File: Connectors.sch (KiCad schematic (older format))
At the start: 4 parts

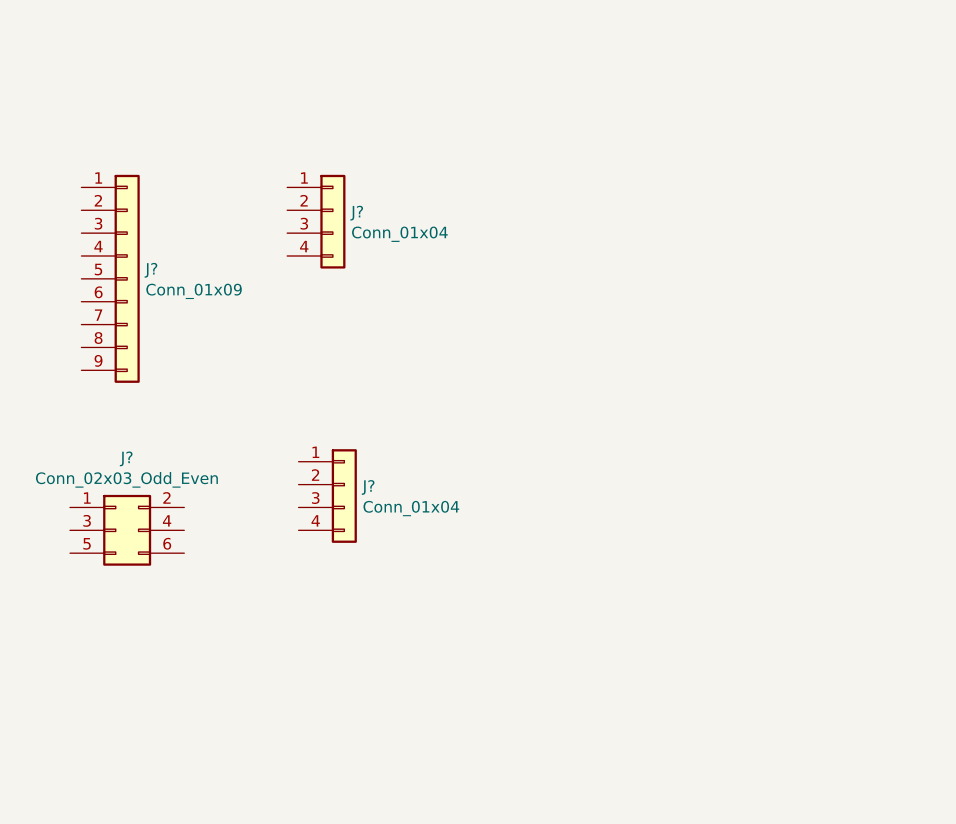
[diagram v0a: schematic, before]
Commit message: Arranged symbols.
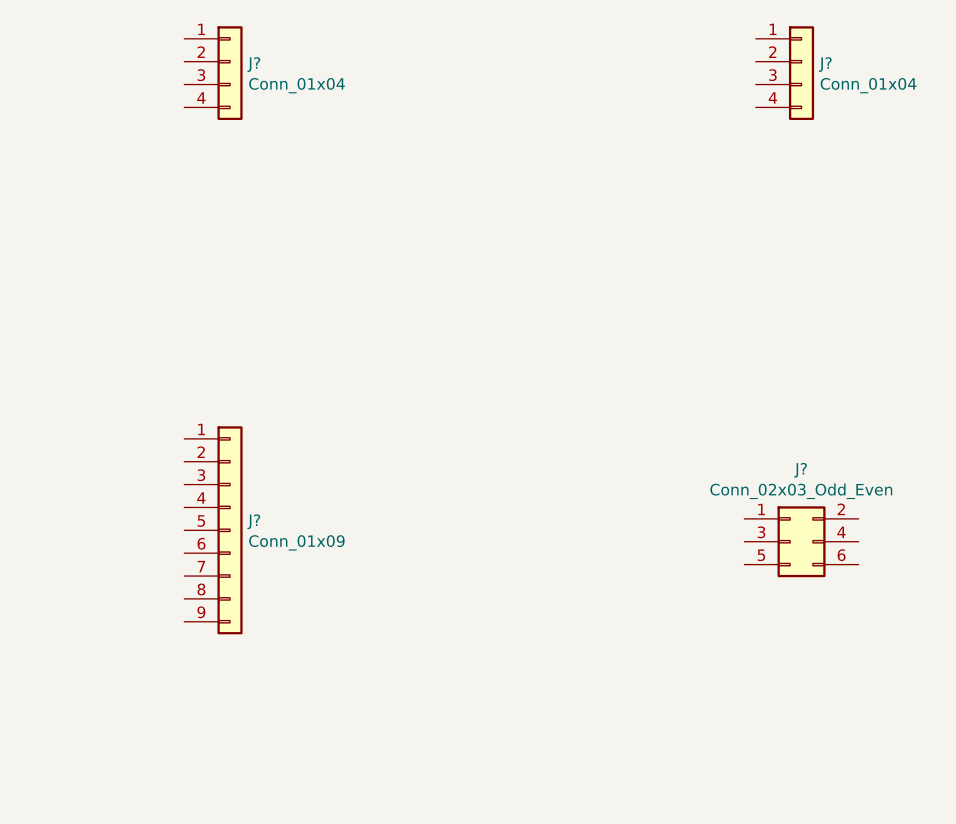
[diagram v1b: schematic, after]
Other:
- moved on the sheet: J?
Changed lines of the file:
@@
 L Connector_Generic:Conn_02x03_Odd_Even J?
 U 1 1 5D848220
-P 4150 3950
-F 0 "J?" H 4200 4267 50  0000 C CNN
-F 1 "Conn_02x03_Odd_Even" H 4200 4176 50  0000 C CNN
-F 2 "" H 4150 3950 50  0001 C CNN
-F 3 "~" H 4150 3950 50  0001 C CNN
-	1    4150 3950
+P 7100 4000
+F 0 "J?" H 7150 4317 50  0000 C CNN
+F 1 "Conn_02x03_Odd_Even" H 7150 4226 50  0000 C CNN
+F 2 "" H 7100 4000 50  0001 C CNN
+F 3 "~" H 7100 4000 50  0001 C CNN
+	1    7100 4000
 	1    0    0    -1
 $EndComp
@@
 L Connector_Generic:Conn_01x04 J?
 U 1 1 5D848B48
-P 5100 2550
-F 0 "J?" H 5180 2542 50  0000 L CNN
-F 1 "Conn_01x04" H 5180 2451 50  0000 L CNN
-F 2 "" H 5100 2550 50  0001 C CNN
-F 3 "~" H 5100 2550 50  0001 C CNN
-	1    5100 2550
+P 4650 1900
+F 0 "J?" H 4730 1892 50  0000 L CNN
+F 1 "Conn_01x04" H 4730 1801 50  0000 L CNN
+F 2 "" H 4650 1900 50  0001 C CNN
+F 3 "~" H 4650 1900 50  0001 C CNN
+	1    4650 1900
 	1    0    0    -1
 $EndComp
@@
 L Connector_Generic:Conn_01x09 J?
 U 1 1 5D8491A9
-P 4200 2850
-F 0 "J?" H 4280 2892 50  0000 L CNN
-F 1 "Conn_01x09" H 4280 2801 50  0000 L CNN
-F 2 "" H 4200 2850 50  0001 C CNN
-F 3 "~" H 4200 2850 50  0001 C CNN
-	1    4200 2850
+P 4650 3950
+F 0 "J?" H 4730 3992 50  0000 L CNN
+F 1 "Conn_01x09" H 4730 3901 50  0000 L CNN
+F 2 "" H 4650 3950 50  0001 C CNN
+F 3 "~" H 4650 3950 50  0001 C CNN
+	1    4650 3950
 	1    0    0    -1
 $EndComp
@@
 L Connector_Generic:Conn_01x04 J?
 U 1 1 5D849E1D
-P 5150 3750
-F 0 "J?" H 5230 3742 50  0000 L CNN
-F 1 "Conn_01x04" H 5230 3651 50  0000 L CNN
-F 2 "" H 5150 3750 50  0001 C CNN
-F 3 "~" H 5150 3750 50  0001 C CNN
-	1    5150 3750
+P 7150 1900
+F 0 "J?" H 7230 1892 50  0000 L CNN
+F 1 "Conn_01x04" H 7230 1801 50  0000 L CNN
+F 2 "" H 7150 1900 50  0001 C CNN
+F 3 "~" H 7150 1900 50  0001 C CNN
+	1    7150 1900
 	1    0    0    -1
 $EndComp

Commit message: Anottated.
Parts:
- gave numbers to parts that had none: 4
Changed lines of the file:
@@
 $EndDescr
 $Comp
-L Connector_Generic:Conn_02x03_Odd_Even J?
+L Connector_Generic:Conn_02x03_Odd_Even J3
 U 1 1 5D848220
 P 7100 4000
-F 0 "J?" H 7150 4317 50  0000 C CNN
+F 0 "J3" H 7150 4317 50  0000 C CNN
 F 1 "Conn_02x03_Odd_Even" H 7150 4226 50  0000 C CNN
 F 2 "" H 7100 4000 50  0001 C CNN
@@
 $EndComp
 $Comp
-L Connector_Generic:Conn_01x04 J?
+L Connector_Generic:Conn_01x04 J1
 U 1 1 5D848B48
 P 4650 1900
-F 0 "J?" H 4730 1892 50  0000 L CNN
+F 0 "J1" H 4730 1892 50  0000 L CNN
 F 1 "Conn_01x04" H 4730 1801 50  0000 L CNN
 F 2 "" H 4650 1900 50  0001 C CNN
@@
 $EndComp
 $Comp
-L Connector_Generic:Conn_01x09 J?
+L Connector_Generic:Conn_01x09 J2
 U 1 1 5D8491A9
 P 4650 3950
-F 0 "J?" H 4730 3992 50  0000 L CNN
+F 0 "J2" H 4730 3992 50  0000 L CNN
 F 1 "Conn_01x09" H 4730 3901 50  0000 L CNN
 F 2 "" H 4650 3950 50  0001 C CNN
@@
 $EndComp
 $Comp
-L Connector_Generic:Conn_01x04 J?
+L Connector_Generic:Conn_01x04 J4
 U 1 1 5D849E1D
 P 7150 1900
-F 0 "J?" H 7230 1892 50  0000 L CNN
+F 0 "J4" H 7230 1892 50  0000 L CNN
 F 1 "Conn_01x04" H 7230 1801 50  0000 L CNN
 F 2 "" H 7150 1900 50  0001 C CNN

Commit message: Added footprints assigments.
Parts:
- J1, J4: footprint (none) -> Connector_PinSocket_2.54mm:PinSocket_1x04_P2.54mm_Vertical
- J2: footprint (none) -> Connector_PinSocket_2.54mm:PinSocket_1x09_P2.54mm_Vertical
- J3: footprint (none) -> Connector_PinSocket_2.54mm:PinSocket_2x03_P2.54mm_Vertical
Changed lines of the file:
@@
 F 0 "J3" H 7150 4317 50  0000 C CNN
 F 1 "Conn_02x03_Odd_Even" H 7150 4226 50  0000 C CNN
-F 2 "" H 7100 4000 50  0001 C CNN
+F 2 "Connector_PinSocket_2.54mm:PinSocket_2x03_P2.54mm_Vertical" H 7100 4000 50  0001 C CNN
 F 3 "~" H 7100 4000 50  0001 C CNN
 	1    7100 4000
@@
 F 0 "J1" H 4730 1892 50  0000 L CNN
 F 1 "Conn_01x04" H 4730 1801 50  0000 L CNN
-F 2 "" H 4650 1900 50  0001 C CNN
+F 2 "Connector_PinSocket_2.54mm:PinSocket_1x04_P2.54mm_Vertical" H 4650 1900 50  0001 C CNN
 F 3 "~" H 4650 1900 50  0001 C CNN
 	1    4650 1900
@@
 F 0 "J2" H 4730 3992 50  0000 L CNN
 F 1 "Conn_01x09" H 4730 3901 50  0000 L CNN
-F 2 "" H 4650 3950 50  0001 C CNN
+F 2 "Connector_PinSocket_2.54mm:PinSocket_1x09_P2.54mm_Vertical" H 4650 3950 50  0001 C CNN
 F 3 "~" H 4650 3950 50  0001 C CNN
 	1    4650 3950
@@
 F 0 "J4" H 7230 1892 50  0000 L CNN
 F 1 "Conn_01x04" H 7230 1801 50  0000 L CNN
-F 2 "" H 7150 1900 50  0001 C CNN
+F 2 "Connector_PinSocket_2.54mm:PinSocket_1x04_P2.54mm_Vertical" H 7150 1900 50  0001 C CNN
 F 3 "~" H 7150 1900 50  0001 C CNN
 	1    7150 1900

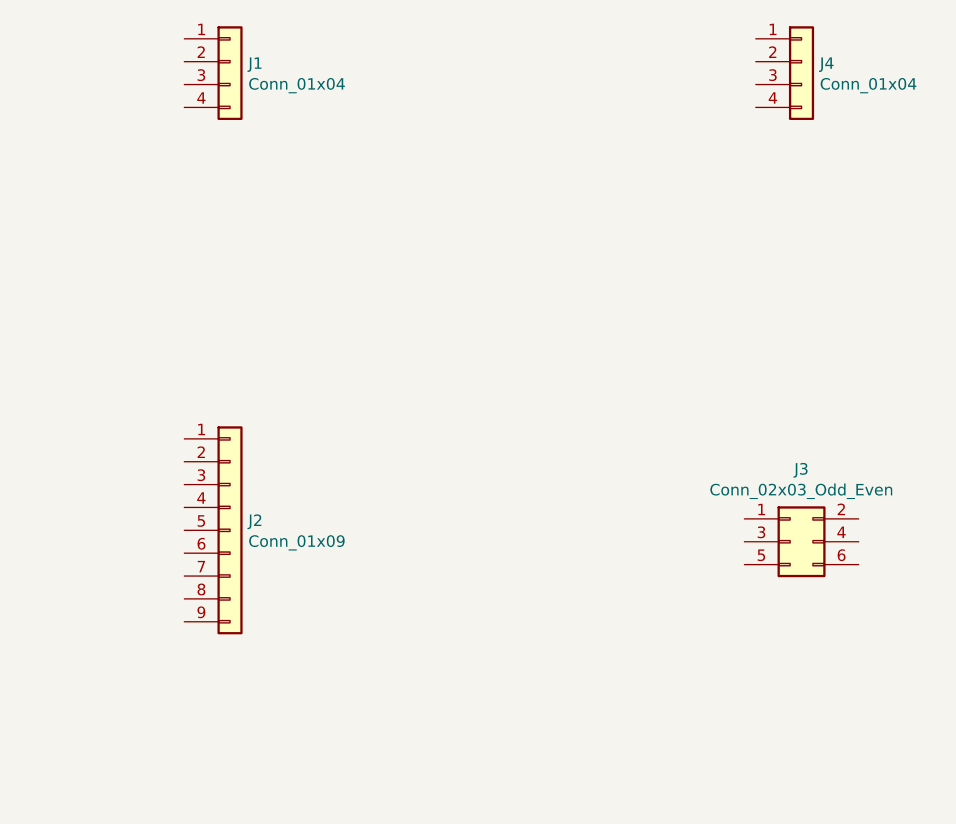
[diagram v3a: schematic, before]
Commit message: Completed asociations and added component values.
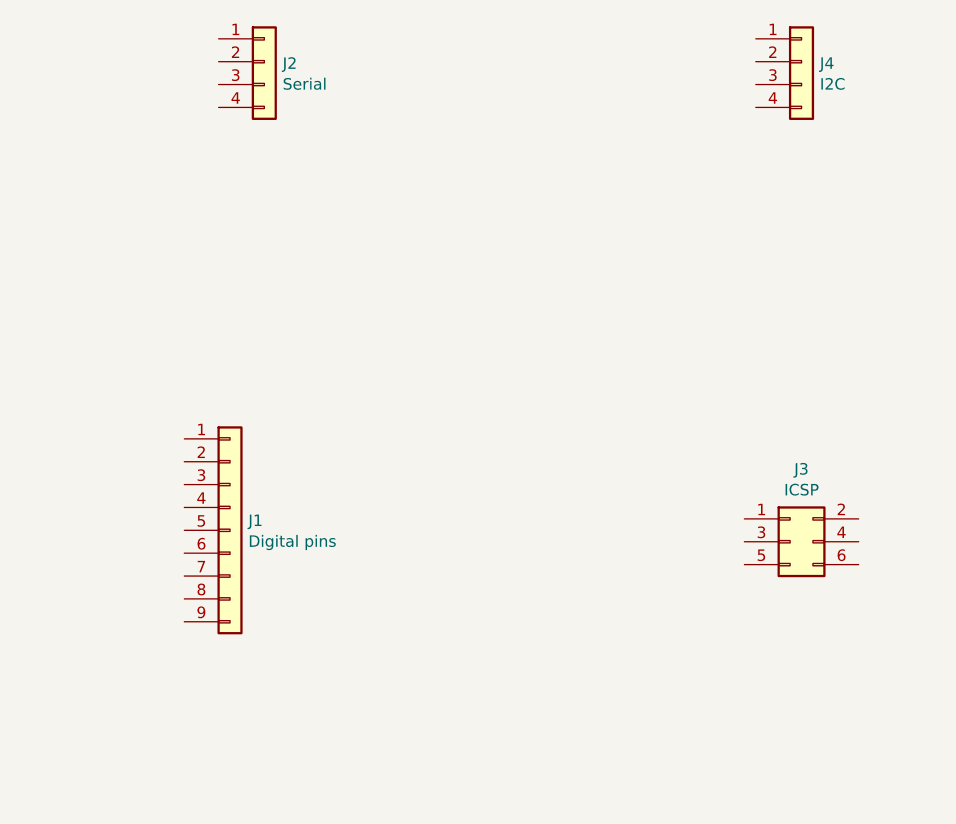
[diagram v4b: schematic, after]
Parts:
- J1: renamed from J2; value Conn_01x09 -> Digital pins
- J2: renamed from J1; value Conn_01x04 -> Serial
- J3: value Conn_02x03_Odd_Even -> ICSP
- J4: value Conn_01x04 -> I2C
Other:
- moved on the sheet: J2
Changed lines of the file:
@@
 P 7100 4000
 F 0 "J3" H 7150 4317 50  0000 C CNN
-F 1 "Conn_02x03_Odd_Even" H 7150 4226 50  0000 C CNN
+F 1 "ICSP" H 7150 4226 50  0000 C CNN
 F 2 "Connector_PinSocket_2.54mm:PinSocket_2x03_P2.54mm_Vertical" H 7100 4000 50  0001 C CNN
 F 3 "~" H 7100 4000 50  0001 C CNN
@@
 $EndComp
 $Comp
-L Connector_Generic:Conn_01x04 J1
+L Connector_Generic:Conn_01x04 J2
 U 1 1 5D848B48
-P 4650 1900
-F 0 "J1" H 4730 1892 50  0000 L CNN
-F 1 "Conn_01x04" H 4730 1801 50  0000 L CNN
-F 2 "Connector_PinSocket_2.54mm:PinSocket_1x04_P2.54mm_Vertical" H 4650 1900 50  0001 C CNN
-F 3 "~" H 4650 1900 50  0001 C CNN
-	1    4650 1900
+P 4800 1900
+F 0 "J2" H 4880 1892 50  0000 L CNN
+F 1 "Serial" H 4880 1801 50  0000 L CNN
+F 2 "Connector_PinSocket_2.54mm:PinSocket_1x04_P2.54mm_Vertical" H 4800 1900 50  0001 C CNN
+F 3 "~" H 4800 1900 50  0001 C CNN
+	1    4800 1900
 	1    0    0    -1
 $EndComp
 $Comp
-L Connector_Generic:Conn_01x09 J2
+L Connector_Generic:Conn_01x09 J1
 U 1 1 5D8491A9
 P 4650 3950
-F 0 "J2" H 4730 3992 50  0000 L CNN
-F 1 "Conn_01x09" H 4730 3901 50  0000 L CNN
+F 0 "J1" H 4730 3992 50  0000 L CNN
+F 1 "Digital pins" H 4730 3901 50  0000 L CNN
 F 2 "Connector_PinSocket_2.54mm:PinSocket_1x09_P2.54mm_Vertical" H 4650 3950 50  0001 C CNN
 F 3 "~" H 4650 3950 50  0001 C CNN
@@
 P 7150 1900
 F 0 "J4" H 7230 1892 50  0000 L CNN
-F 1 "Conn_01x04" H 7230 1801 50  0000 L CNN
+F 1 "I2C" H 7230 1801 50  0000 L CNN
 F 2 "Connector_PinSocket_2.54mm:PinSocket_1x04_P2.54mm_Vertical" H 7150 1900 50  0001 C CNN
 F 3 "~" H 7150 1900 50  0001 C CNN

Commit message: Completed wiring and connectors sheet.
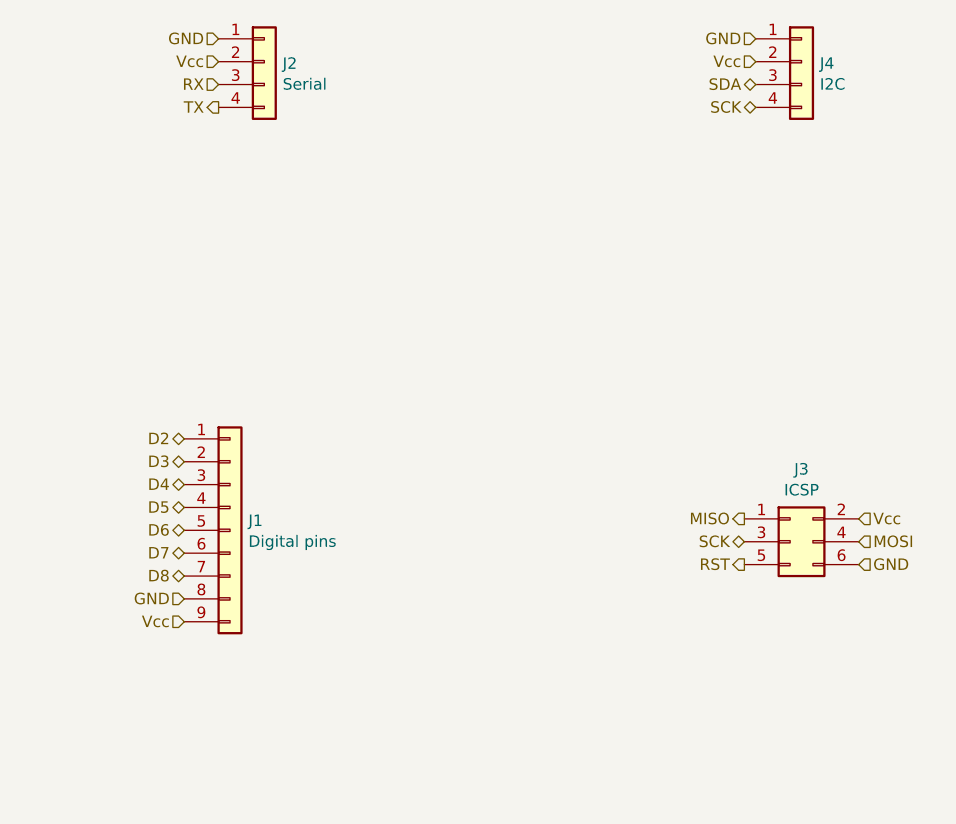
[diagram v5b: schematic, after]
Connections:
- net MISO: now reaches J3.1 (Pin_1)
- net Vcc: now reaches J3.2 (Pin_2)
- net Vcc: now also J1.9 (Pin_9), J2.2 (Pin_2), J4.2 (Pin_2)
- net SCK: now reaches J3.3 (Pin_3)
- net SCK: now also J4.4 (Pin_4)
- net MOSI: now reaches J3.4 (Pin_4)
- net RST: now reaches J3.5 (Pin_5)
- net GND: now reaches J3.6 (Pin_6)
- net GND: now also J1.8 (Pin_8), J2.1 (Pin_1), J4.1 (Pin_1)
- net RX: now reaches J2.3 (Pin_3)
- net TX: now reaches J2.4 (Pin_4)
- net D2: now reaches J1.1 (Pin_1)
- net D3: now reaches J1.2 (Pin_2)
- net D4: now reaches J1.3 (Pin_3)
- net D5: now reaches J1.4 (Pin_4)
- net D6: now reaches J1.5 (Pin_5)
- net D7: now reaches J1.6 (Pin_6)
- net D8: now reaches J1.7 (Pin_7)
- net SDA: now reaches J4.3 (Pin_3)
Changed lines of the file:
@@
 	1    0    0    -1
 $EndComp
+Text HLabel 6900 3900 0    50   Output ~ 0
+MISO
+Text HLabel 6900 4000 0    50   BiDi ~ 0
+SCK
+Text HLabel 6900 4100 0    50   Output ~ 0
+RST
+Text HLabel 7400 3900 2    50   Input ~ 0
+Vcc
+Text HLabel 7400 4000 2    50   Input ~ 0
+MOSI
+Text HLabel 7400 4100 2    50   Input ~ 0
+GND
+Text HLabel 4600 1800 0    50   Input ~ 0
+GND
+Text HLabel 4600 1900 0    50   Input ~ 0
+Vcc
+Text HLabel 4600 2000 0    50   Input ~ 0
+RX
+Text HLabel 4600 2100 0    50   Output ~ 0
+TX
+Text HLabel 6950 1800 0    50   Input ~ 0
+GND
+Text HLabel 6950 1900 0    50   Input ~ 0
+Vcc
+Text HLabel 6950 2000 0    50   BiDi ~ 0
+SDA
+Text HLabel 4450 3550 0    50   BiDi ~ 0
+D2
+Text HLabel 4450 3650 0    50   BiDi ~ 0
+D3
+Text HLabel 4450 3750 0    50   BiDi ~ 0
+D4
+Text HLabel 4450 3850 0    50   BiDi ~ 0
+D5
+Text HLabel 4450 3950 0    50   BiDi ~ 0
+D6
+Text HLabel 4450 4050 0    50   BiDi ~ 0
+D7
+Text HLabel 4450 4150 0    50   BiDi ~ 0
+D8
+Text HLabel 4450 4250 0    50   Input ~ 0
+GND
+Text HLabel 4450 4350 0    50   Input ~ 0
+Vcc
+Text HLabel 6950 2100 0    50   BiDi ~ 0
+SCK
 $EndSCHEMATC

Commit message: Added functional block description.
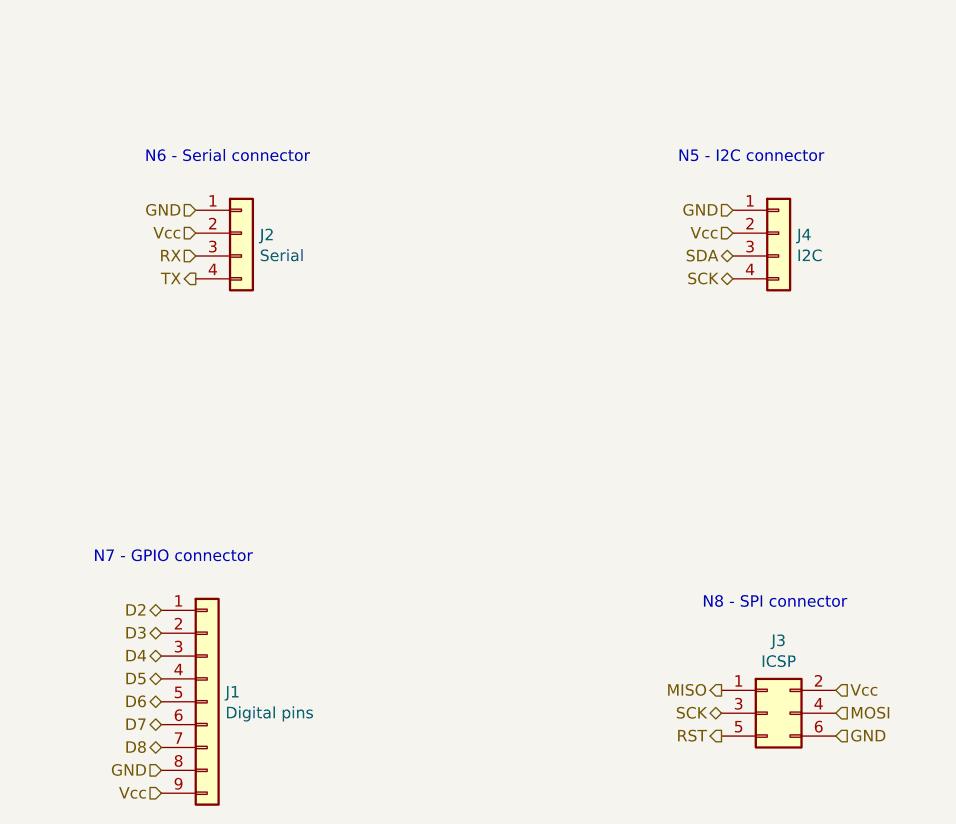
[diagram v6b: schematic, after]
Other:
- note added: "N5 - I2C connector"
- note added: "N6 - Serial connector\n"
- note added: "N7 - GPIO connector"
- note added: "N8 - SPI connector"
- moved on the sheet: J1, J2, J3, J4
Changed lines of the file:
@@
 L Connector_Generic:Conn_02x03_Odd_Even J3
 U 1 1 5D848220
-P 7100 4000
-F 0 "J3" H 7150 4317 50  0000 C CNN
-F 1 "ICSP" H 7150 4226 50  0000 C CNN
-F 2 "Connector_PinSocket_2.54mm:PinSocket_2x03_P2.54mm_Vertical" H 7100 4000 50  0001 C CNN
-F 3 "~" H 7100 4000 50  0001 C CNN
-	1    7100 4000
+P 7000 4750
+F 0 "J3" H 7050 5067 50  0000 C CNN
+F 1 "ICSP" H 7050 4976 50  0000 C CNN
+F 2 "Connector_PinSocket_2.54mm:PinSocket_2x03_P2.54mm_Vertical" H 7000 4750 50  0001 C CNN
+F 3 "~" H 7000 4750 50  0001 C CNN
+	1    7000 4750
 	1    0    0    -1
 $EndComp
@@
 L Connector_Generic:Conn_01x04 J2
 U 1 1 5D848B48
-P 4800 1900
-F 0 "J2" H 4880 1892 50  0000 L CNN
-F 1 "Serial" H 4880 1801 50  0000 L CNN
-F 2 "Connector_PinSocket_2.54mm:PinSocket_1x04_P2.54mm_Vertical" H 4800 1900 50  0001 C CNN
-F 3 "~" H 4800 1900 50  0001 C CNN
-	1    4800 1900
+P 4700 2650
+F 0 "J2" H 4780 2642 50  0000 L CNN
+F 1 "Serial" H 4780 2551 50  0000 L CNN
+F 2 "Connector_PinSocket_2.54mm:PinSocket_1x04_P2.54mm_Vertical" H 4700 2650 50  0001 C CNN
+F 3 "~" H 4700 2650 50  0001 C CNN
+	1    4700 2650
 	1    0    0    -1
 $EndComp
@@
 L Connector_Generic:Conn_01x09 J1
 U 1 1 5D8491A9
-P 4650 3950
-F 0 "J1" H 4730 3992 50  0000 L CNN
-F 1 "Digital pins" H 4730 3901 50  0000 L CNN
-F 2 "Connector_PinSocket_2.54mm:PinSocket_1x09_P2.54mm_Vertical" H 4650 3950 50  0001 C CNN
-F 3 "~" H 4650 3950 50  0001 C CNN
-	1    4650 3950
+P 4550 4700
+F 0 "J1" H 4630 4742 50  0000 L CNN
+F 1 "Digital pins" H 4630 4651 50  0000 L CNN
+F 2 "Connector_PinSocket_2.54mm:PinSocket_1x09_P2.54mm_Vertical" H 4550 4700 50  0001 C CNN
+F 3 "~" H 4550 4700 50  0001 C CNN
+	1    4550 4700
 	1    0    0    -1
 $EndComp
@@
 L Connector_Generic:Conn_01x04 J4
 U 1 1 5D849E1D
-P 7150 1900
-F 0 "J4" H 7230 1892 50  0000 L CNN
-F 1 "I2C" H 7230 1801 50  0000 L CNN
-F 2 "Connector_PinSocket_2.54mm:PinSocket_1x04_P2.54mm_Vertical" H 7150 1900 50  0001 C CNN
-F 3 "~" H 7150 1900 50  0001 C CNN
-	1    7150 1900
+P 7050 2650
+F 0 "J4" H 7130 2642 50  0000 L CNN
+F 1 "I2C" H 7130 2551 50  0000 L CNN
+F 2 "Connector_PinSocket_2.54mm:PinSocket_1x04_P2.54mm_Vertical" H 7050 2650 50  0001 C CNN
+F 3 "~" H 7050 2650 50  0001 C CNN
+	1    7050 2650
 	1    0    0    -1
 $EndComp
-Text HLabel 6900 3900 0    50   Output ~ 0
+Text HLabel 6800 4650 0    50   Output ~ 0
 MISO
-Text HLabel 6900 4000 0    50   BiDi ~ 0
+Text HLabel 6800 4750 0    50   BiDi ~ 0
 SCK
-Text HLabel 6900 4100 0    50   Output ~ 0
+Text HLabel 6800 4850 0    50   Output ~ 0
 RST
-Text HLabel 7400 3900 2    50   Input ~ 0
+Text HLabel 7300 4650 2    50   Input ~ 0
 Vcc
-Text HLabel 7400 4000 2    50   Input ~ 0
+Text HLabel 7300 4750 2    50   Input ~ 0
 MOSI
-Text HLabel 7400 4100 2    50   Input ~ 0
+Text HLabel 7300 4850 2    50   Input ~ 0
 GND
-Text HLabel 4600 1800 0    50   Input ~ 0
+Text HLabel 4500 2550 0    50   Input ~ 0
 GND
-Text HLabel 4600 1900 0    50   Input ~ 0
+Text HLabel 4500 2650 0    50   Input ~ 0
 Vcc
-Text HLabel 4600 2000 0    50   Input ~ 0
+Text HLabel 4500 2750 0    50   Input ~ 0
 RX
-Text HLabel 4600 2100 0    50   Output ~ 0
+Text HLabel 4500 2850 0    50   Output ~ 0
 TX
-Text HLabel 6950 1800 0    50   Input ~ 0
+Text HLabel 6850 2550 0    50   Input ~ 0
 GND
-Text HLabel 6950 1900 0    50   Input ~ 0
+Text HLabel 6850 2650 0    50   Input ~ 0
 Vcc
-Text HLabel 6950 2000 0    50   BiDi ~ 0
+Text HLabel 6850 2750 0    50   BiDi ~ 0
 SDA
-Text HLabel 4450 3550 0    50   BiDi ~ 0
+Text HLabel 4350 4300 0    50   BiDi ~ 0
 D2
-Text HLabel 4450 3650 0    50   BiDi ~ 0
+Text HLabel 4350 4400 0    50   BiDi ~ 0
 D3
-Text HLabel 4450 3750 0    50   BiDi ~ 0
+Text HLabel 4350 4500 0    50   BiDi ~ 0
 D4
-Text HLabel 4450 3850 0    50   BiDi ~ 0
+Text HLabel 4350 4600 0    50   BiDi ~ 0
 D5
-Text HLabel 4450 3950 0    50   BiDi ~ 0
+Text HLabel 4350 4700 0    50   BiDi ~ 0
 D6
-Text HLabel 4450 4050 0    50   BiDi ~ 0
+Text HLabel 4350 4800 0    50   BiDi ~ 0
 D7
-Text HLabel 4450 4150 0    50   BiDi ~ 0
+Text HLabel 4350 4900 0    50   BiDi ~ 0
 D8
-Text HLabel 4450 4250 0    50   Input ~ 0
+Text HLabel 4350 5000 0    50   Input ~ 0
 GND
-Text HLabel 4450 4350 0    50   Input ~ 0
+Text HLabel 4350 5100 0    50   Input ~ 0
 Vcc
-Text HLabel 6950 2100 0    50   BiDi ~ 0
+Text HLabel 6850 2850 0    50   BiDi ~ 0
 SCK
+Text Notes 5000 2350 2    50   ~ 0
+N6 - Serial connector\n
+Text Notes 7250 2350 2    50   ~ 0
+N5 - I2C connector
+Text Notes 4750 4100 2    50   ~ 0
+N7 - GPIO connector
+Text Notes 7350 4300 2    50   ~ 0
+N8 - SPI connector
 $EndSCHEMATC
